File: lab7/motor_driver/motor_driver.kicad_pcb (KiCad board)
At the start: 2 copper layers, 80 x 80 mm, 22 parts, among them J1 BATTERY, J2 MOTOR_01, J3 MOTOR_02, Q1 IRLB8721PBF, Q2 IRLB8721PBF, U1 ESP32-C3-SuperMini

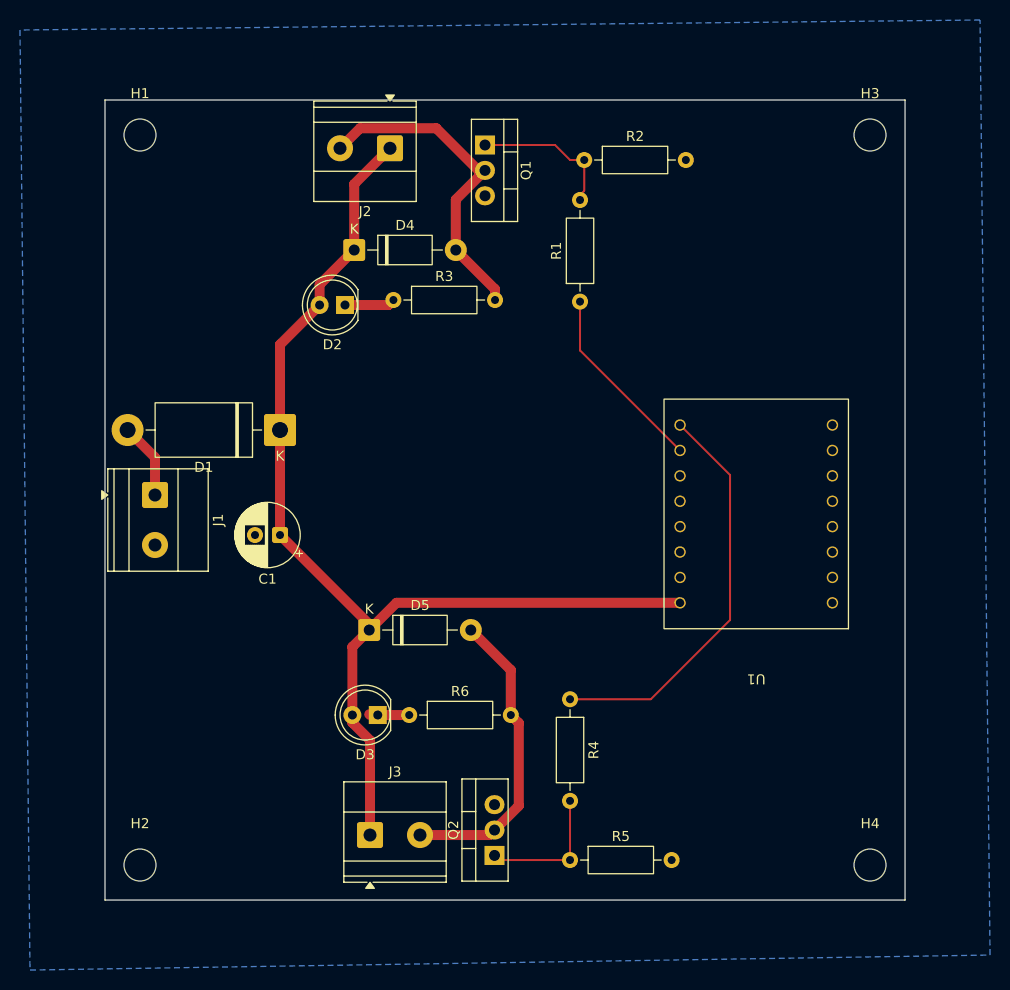
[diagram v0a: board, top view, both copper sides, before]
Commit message: Shrink board size; fix clearance issues
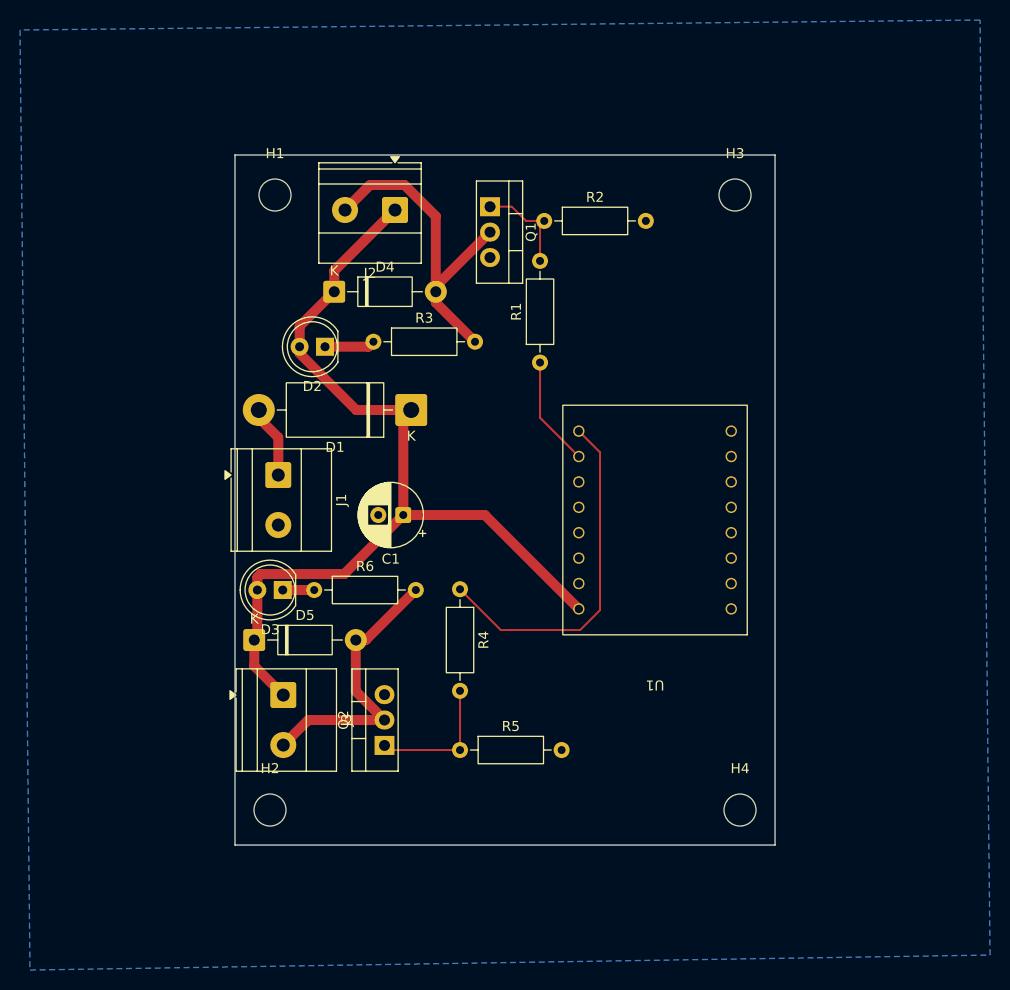
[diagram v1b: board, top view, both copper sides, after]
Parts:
- moved J3 16.5 mm to (181.3, 103.5), turned to -90 degrees
- moved D3 15.7 mm to (181.3, 93.0)
- moved R6 15.7 mm to (184.4, 93.0)
- moved Q2 15.6 mm to (191.4, 108.5)
- moved R4 15.6 mm to (199.0, 92.9)
- moved R5 15.6 mm to (199.0, 109.0)
- moved H1 14.8 mm to (180.5, 53.5)
- moved H3 14.8 mm to (226.5, 53.5)
- moved H2 14.1 mm to (180.0, 115.0)
- moved H4 14.1 mm to (227.0, 115.0)
- moved D1 13.3 mm to (194.1, 75.0)
- moved C1 12.5 mm to (193.3, 85.5)
- moved J1 12.5 mm to (180.8, 81.5)
- moved D5 11.5 mm to (178.4, 98.0)
- moved U1 10.1 mm to (218.5, 86.0)
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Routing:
- net +6V: track 110.6 -> 94.3 mm
- net Net-(U1-GPIO1): track 19.0 -> 11.5 mm
- net Net-(U1-GPIO0): track 40.9 -> 35.3 mm
- net Net-(Q1-G): track 14.7 -> 10.2 mm
- net Net-(D5-A): track 30.7 -> 28.4 mm
- net Net-(D4-A): track 32.9 -> 33.8 mm
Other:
- board size 80 x 80 mm -> 54 x 69 mm

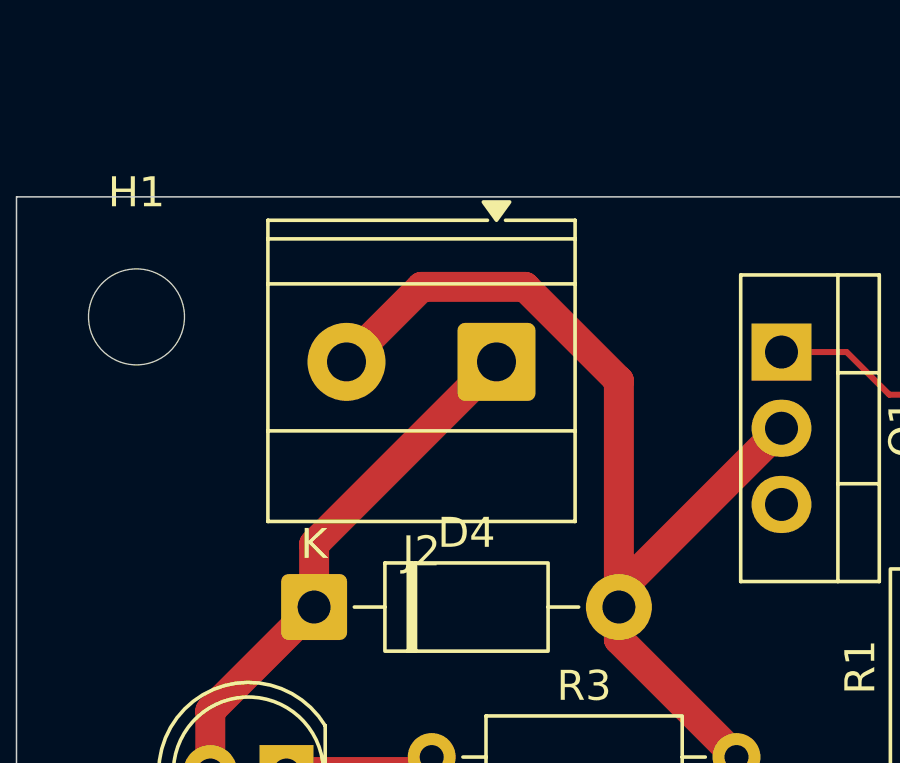
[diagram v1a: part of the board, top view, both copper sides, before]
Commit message: Scooch J2 closer to edge to fix error from autograder
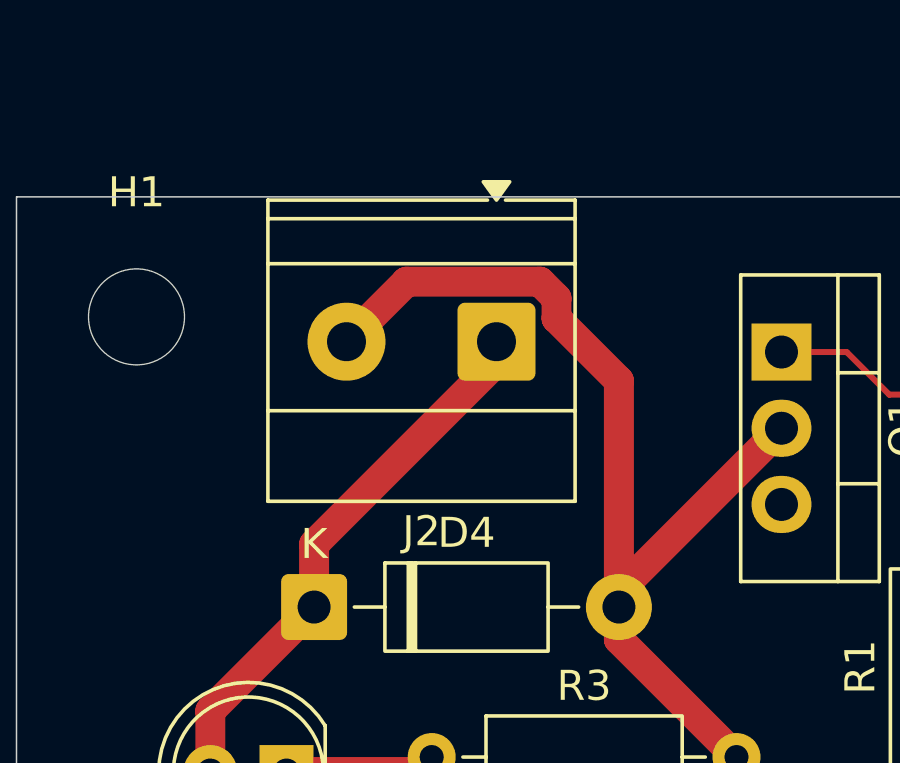
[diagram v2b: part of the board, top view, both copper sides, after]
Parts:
- moved J2 0.67 mm to (192.5, 54.3)
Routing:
- net +6V: track 94.3 -> 95.0 mm
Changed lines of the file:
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@@
 	(footprint "TerminalBlock_Phoenix:TerminalBlock_Phoenix_MKDS-1,5-2_1x02_P5.00mm_Horizontal"
 		(layer "F.Cu")
-		(at 192.5 55 180)
+		(at 192.5 54.3275 180)
 		(descr "Terminal Block Phoenix MKDS-1,5-2, 2 pins, pitch 5mm, size 10x9.8mm, drill diameter 1.3mm, pad diameter 2.6mm, http://www.farnell.com/datasheets/100425.pdf")
 		(tags "THT Terminal Block Phoenix MKDS-1,5-2 pitch 5mm size 10x9.8mm drill 1.3mm pad 2.6mm")
@@
 	)
 	(segment
+		(start 192.5 55)
+		(end 192.5 54.3275)
+		(width 1)
+		(layer "F.Cu")
+		(net "+6V")
+	)
+	(segment
 		(start 186.42 61.08)
 		(end 192.5 55)
@@
 	)
 	(segment
+		(start 186.42 63.1725)
+		(end 186.42 61.08)
+		(width 1)
+		(layer "F.Cu")
+		(net "+6V")
+	)
+	(segment
 		(start 178.735 91.727208)
 		(end 178.735 93)
@@
 	)
 	(segment
-		(start 186.42 63.1725)
-		(end 186.42 61.08)
-		(width 1)
-		(layer "F.Cu")
-		(net "+6V")
-	)
-	(segment
 		(start 194.12 75)
 		(end 188.6275 75)
@@
 	)
 	(segment
-		(start 193.45043 52.5)
-		(end 196.58 55.62957)
+		(start 194.5 52.87707)
+		(end 194.5 53.54957)
+		(width 1)
+		(layer "F.Cu")
+		(net "Net-(D4-A)")
+	)
+	(segment
+		(start 193.95043 52.3275)
+		(end 194.5 52.87707)
+		(width 1)
+		(layer "F.Cu")
+		(net "Net-(D4-A)")
+	)
+	(segment
+		(start 187.5 54.3275)
+		(end 189.5 52.3275)
 		(width 1)
 		(layer "F.Cu")
@@
 	)
 	(segment
-		(start 190 52.5)
-		(end 193.45043 52.5)
+		(start 196.58 55.62957)
+		(end 196.58 63.1725)
 		(width 1)
 		(layer "F.Cu")
@@
 	)
 	(segment
-		(start 196.58 64.2525)
-		(end 200.5 68.1725)
+		(start 189.5 52.3275)
+		(end 193.95043 52.3275)
 		(width 1)
 		(layer "F.Cu")
@@
 	)
 	(segment
-		(start 196.58 55.62957)
-		(end 196.58 63.1725)
+		(start 196.58 64.2525)
+		(end 200.5 68.1725)
 		(width 1)
 		(layer "F.Cu")
@@
 	)
 	(segment
-		(start 187.5 55)
-		(end 190 52.5)
+		(start 194.5 53.54957)
+		(end 196.58 55.62957)
 		(width 1)
 		(layer "F.Cu")
